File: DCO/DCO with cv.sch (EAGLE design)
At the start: 24 parts, among them IC1 PIC16F18325SL, IC2 MAX5216, IC3 TL082D, IC4 TL082D, Q1 MMBT3906

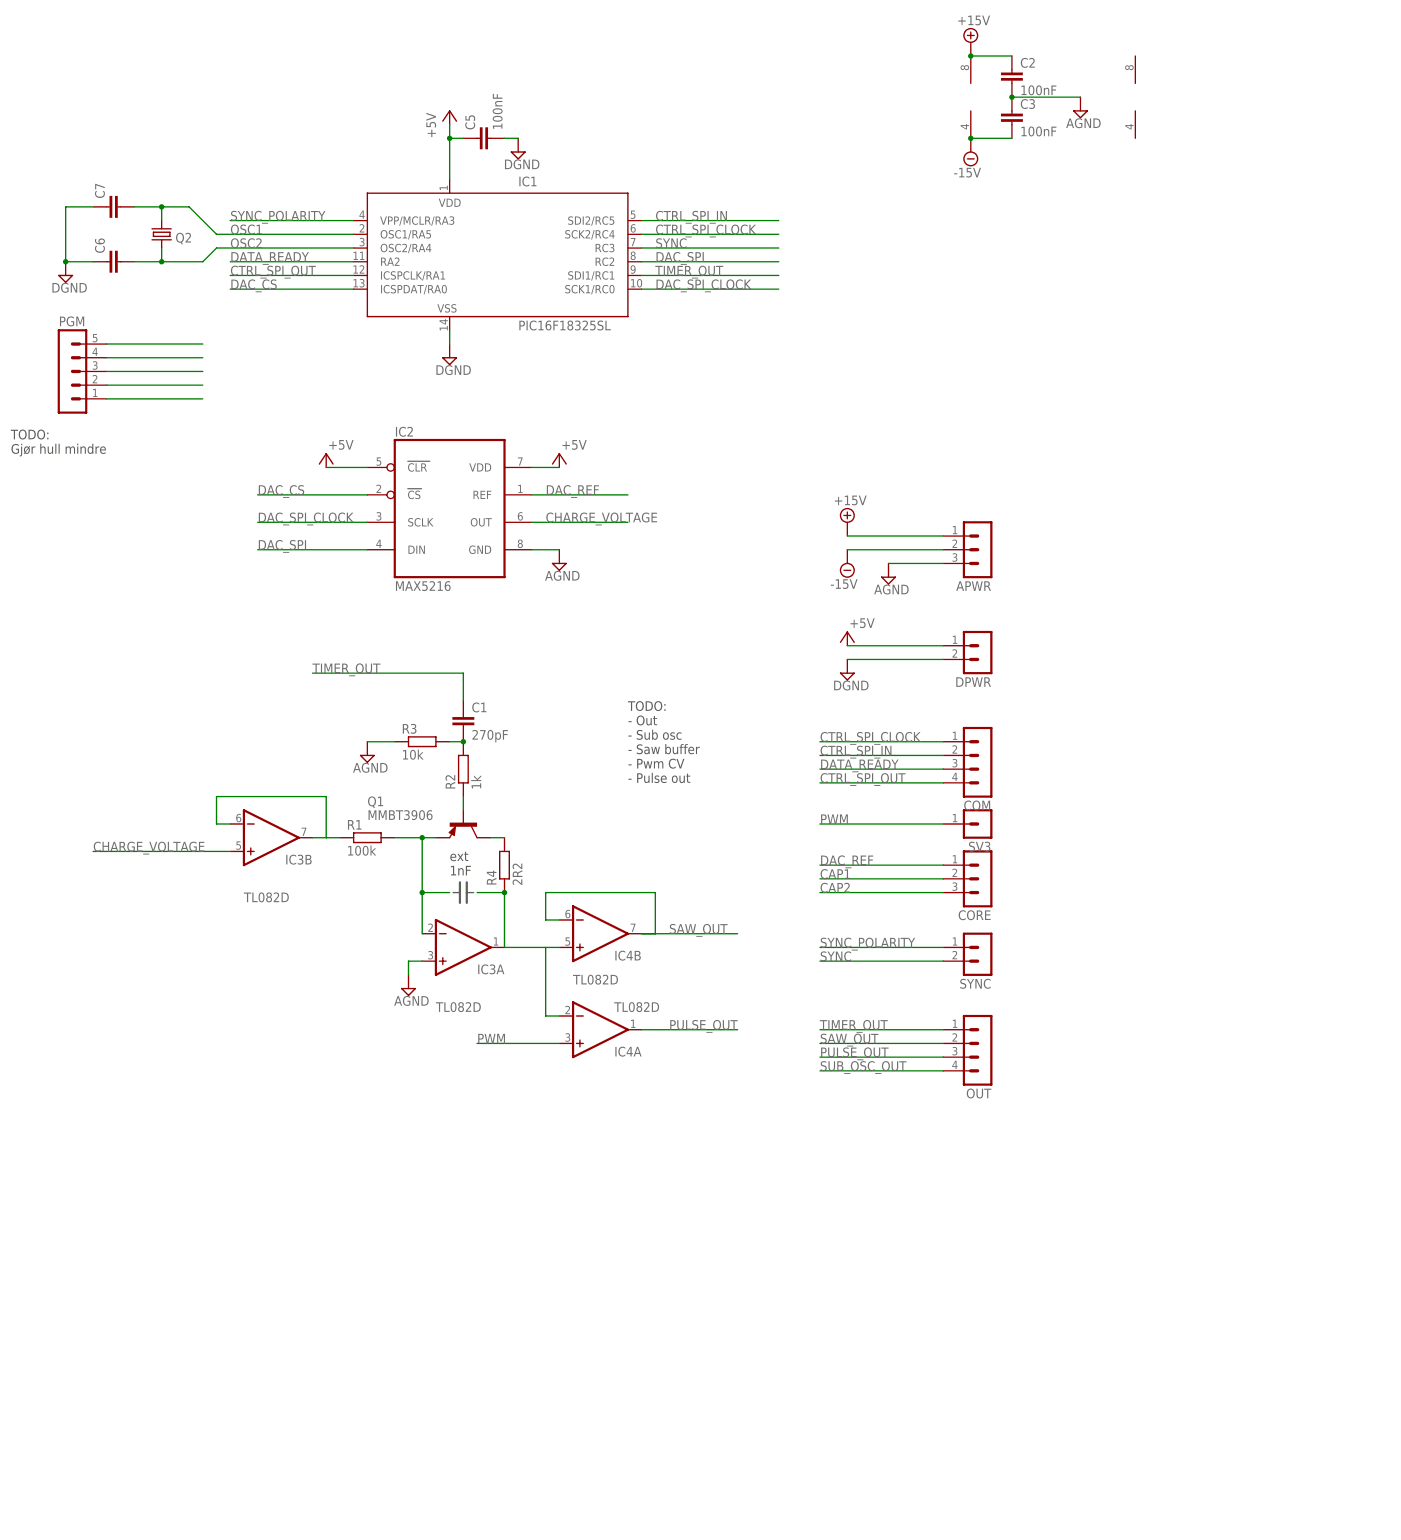
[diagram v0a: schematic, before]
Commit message: Partially complete layout for DCO with CV control for pulse and sub osc, and separate triangle wave former
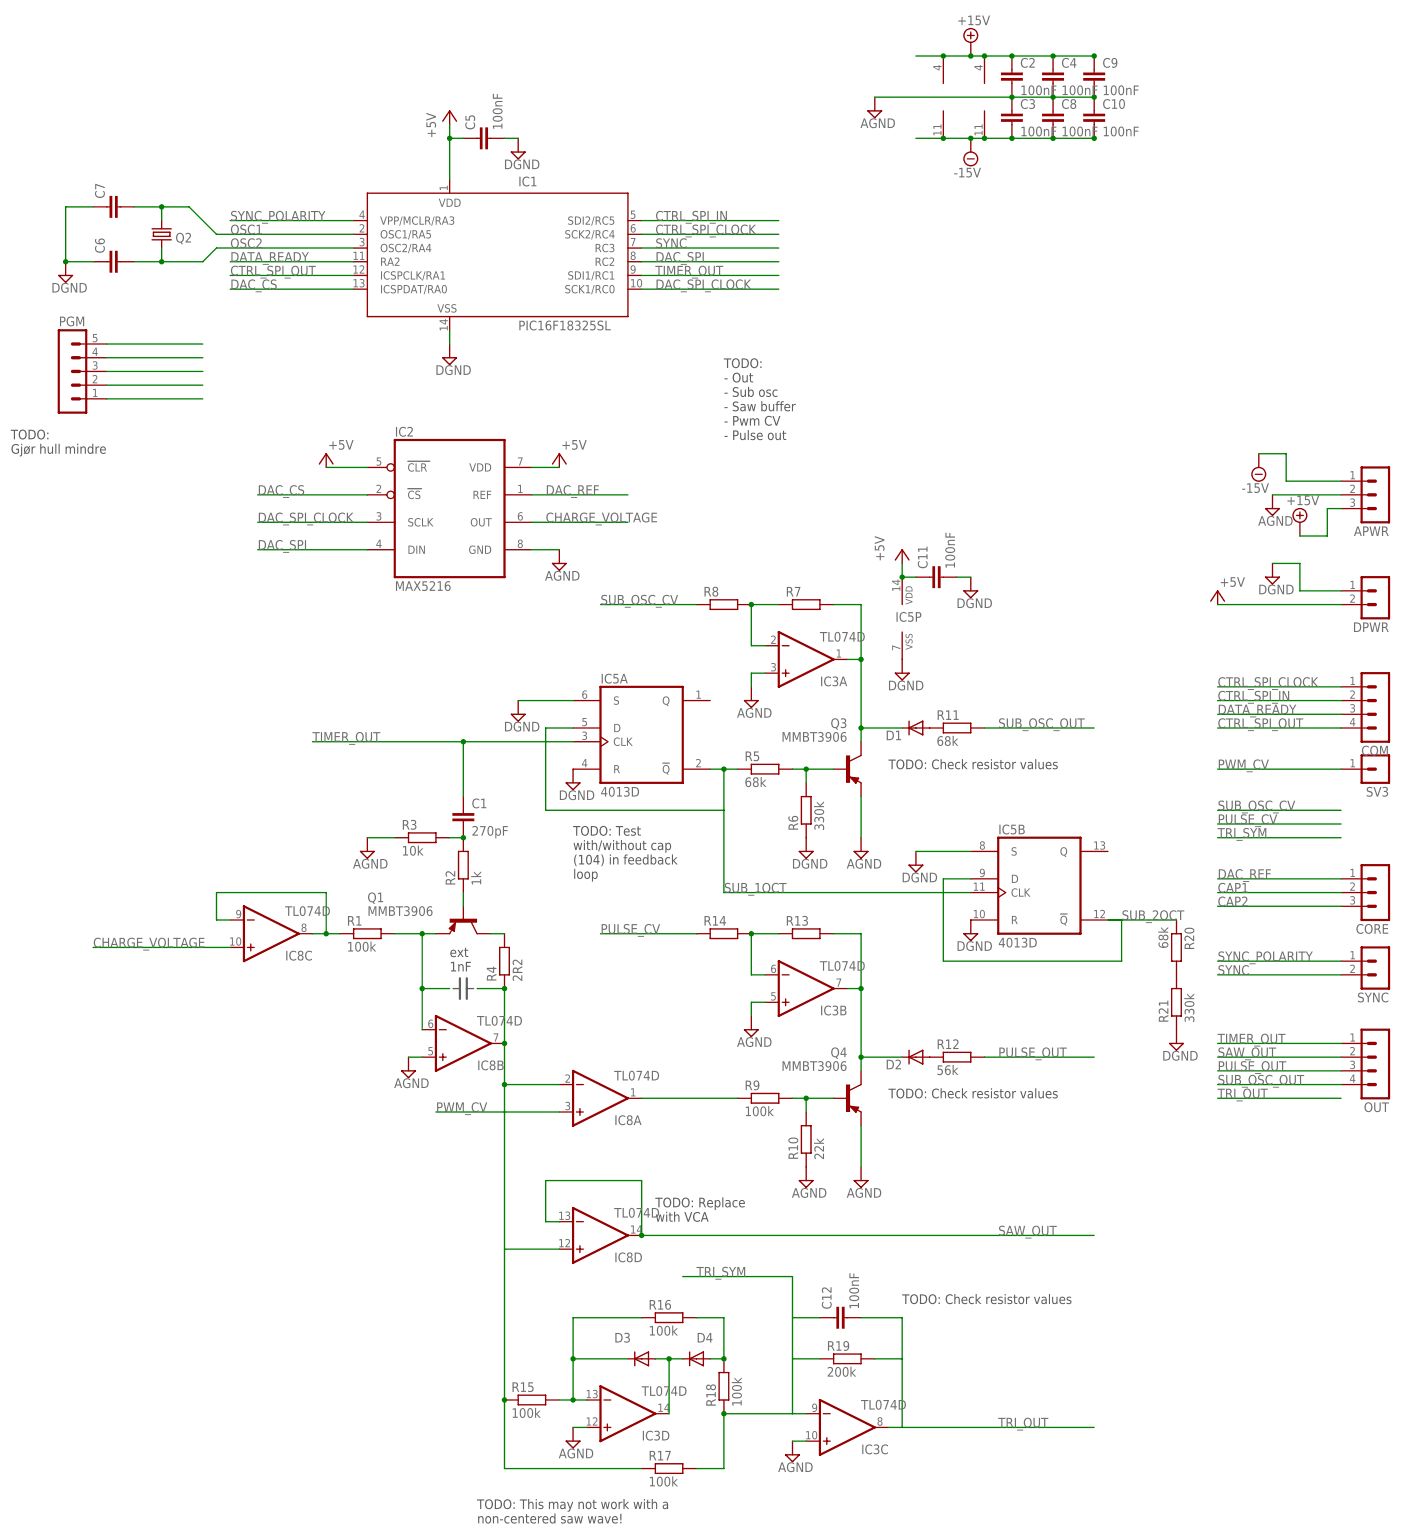
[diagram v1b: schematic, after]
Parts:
- removed IC4: TL082D, linear:TL082D
- added C10, C11, C12, C4, C8, C9: 100nF, resistor:C-EUC0805
- added D1, D2, D3, D4: (no value), diode:DIODE-SOD80C
- added IC5: 4013D, joakim:4013D
- added IC8: TL074D, linear:TL074D
- added Q3, Q4: MMBT3906, transistor-pnp:MMBT3906LT1SMD
- added R10: 22k, resistor:R-EU_R0805
- added R11, R20, R5: 68k, resistor:R-EU_R0805
- added R12: 56k, resistor:R-EU_R0805
- added R13, R14, R7, R8: (no value), resistor:R-EU_R0805
- added R15, R16, R17, R18, R9: 100k, resistor:R-EU_R0805
- added R19: 200k, resistor:R-EU_R0805
- added R21, R6: 330k, resistor:R-EU_R0805
- IC3: value TL082D -> TL074D; device linear:TL082D -> linear:TL074D
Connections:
- removed net PWM: IC4A.+IN, SV3.1
- new net +15V1: C4.1
- new net +15V2: C9.1
- new net -15V1: C8.2
- new net -15V2: C10.2
- new net N$1: R20.2, R21.2
- new net N$11: Q3.B, R5.2, R6.2
- new net N$12: D1.C, IC3A.OUT, Q3.C, R7.2
- new net N$13: IC8A.OUT, R9.1
- new net N$14: Q4.B, R10.2, R9.2
- new net N$15: IC3A.-IN, R7.1, R8.2
- new net N$16: D2.C, IC3B.OUT, Q4.C, R13.2
- new net N$17: D1.A, R11.1
- new net N$18: D2.A, R12.1
- new net N$19: D3.C, IC3D.-IN, R15.2, R16.1
- new net N$20: IC3B.-IN, R13.1, R14.2
- new net N$23: D3.A, D4.C, IC3D.OUT
- new net N$24: D4.A, R16.2, R18.2
- new net PULSE_CV: R14.1
- new net PWM_CV: IC8A.+IN, SV3.1
- new net SUB_1OCT: IC5A.!Q, IC5A.D, IC5B.CLK, R5.1
- new net SUB_2OCT: IC5B.!Q, IC5B.D, R20.1
- new net SUB_OSC_CV: R8.1
- new net TRI_OUT: C12.2, IC3C.OUT, R19.2
- new net TRI_SYM: C12.1, IC3C.-IN, R17.2, R18.1, R19.1
- net +15V: now also APWR.3, IC8P.V+; no longer APWR.1
- net +5V: now also C11.1, DPWR.2, IC5P.VDD; no longer DPWR.1
- net -15V: now also APWR.1, IC8P.V-; no longer APWR.2
- net AGND: now also APWR.2, C10.1, C4.2, C8.1, C9.2, IC3B.+IN, IC3C.+IN, IC3D.+IN, IC8B.+IN, Q3.E, Q4.E, R10.1; no longer APWR.3
- net CAP1: now also IC8B.-IN; no longer IC3A.-IN
- net CAP2: now also IC8A.-IN, IC8B.OUT, IC8D.+IN, R15.1, R17.1; no longer IC3A.OUT, IC4A.-IN, IC4B.+IN
- net CHARGE_VOLTAGE: now also IC8C.+IN; no longer IC3B.+IN
- net DGND: now also C11.2, DPWR.1, IC5A.R, IC5A.S, IC5B.R, IC5B.S, IC5P.VSS, R21.1, R6.1; no longer DPWR.2
- net N$10: now also IC8C.-IN, IC8C.OUT; no longer IC3B.-IN, IC3B.OUT
- net PULSE_OUT: now also R12.2; no longer IC4A.OUT
- net SAW_OUT: now also IC8D.-IN, IC8D.OUT; no longer IC4B.-IN, IC4B.OUT
- net SUB_OSC_OUT: now also R11.2
- net TIMER_OUT: now also IC5A.CLK
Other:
- note added: "TODO: Check resistor values"
- note added: "TODO: Replace with VCA"
- note added: "TODO: Test with/without cap (104) in feedback loop"
- note added: "TODO: This may not work with a non-centered saw wave!"
- moved on the sheet: APWR, C1, COM, CORE, DPWR, IC3A, IC3B, OUT, Q1, R1, R2, R3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
